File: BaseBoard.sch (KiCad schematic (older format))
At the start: 170 parts, among them Q1 MMBT2222A-7-F, Q10 IRLML6401TRPBF, Q11 MMBT2222A-7-F, Q12 IRLML6401TRPBF, Q13 MMBT2222A-7-F, Q14 IRLML6401TRPBF, Q15 MMBT2222A-7-F, Q16 IRLML6401TRPBF, Q2 IRLML6401TRPBF, Q3 MMBT2222A-7-F, Q4 IRLML6401TRPBF, Q5 MMBT2222A-7-F, Q6 IRLML6401TRPBF, Q7 MMBT2222A-7-F, Q8 IRLML6401TRPBF, Q9 MMBT2222A-7-F, U1 TLC5971PWPR, U10 TLC5971PWPR, U11 TLC5971PWPR, U12 TLC5971PWPR, U13 TLC5971PWPR, U14 TLC5971PWPR, U15 TLC5971PWPR, U16 TLC5971PWPR, U2 TLC5971PWPR, U3 TLC5971PWPR, U4 TLC5971PWPR, U5 TLC5971PWPR, U6 TLC5971PWPR, U7 TLC5971PWPR, U8 TLC5971PWPR, U9 TLC5971PWPR

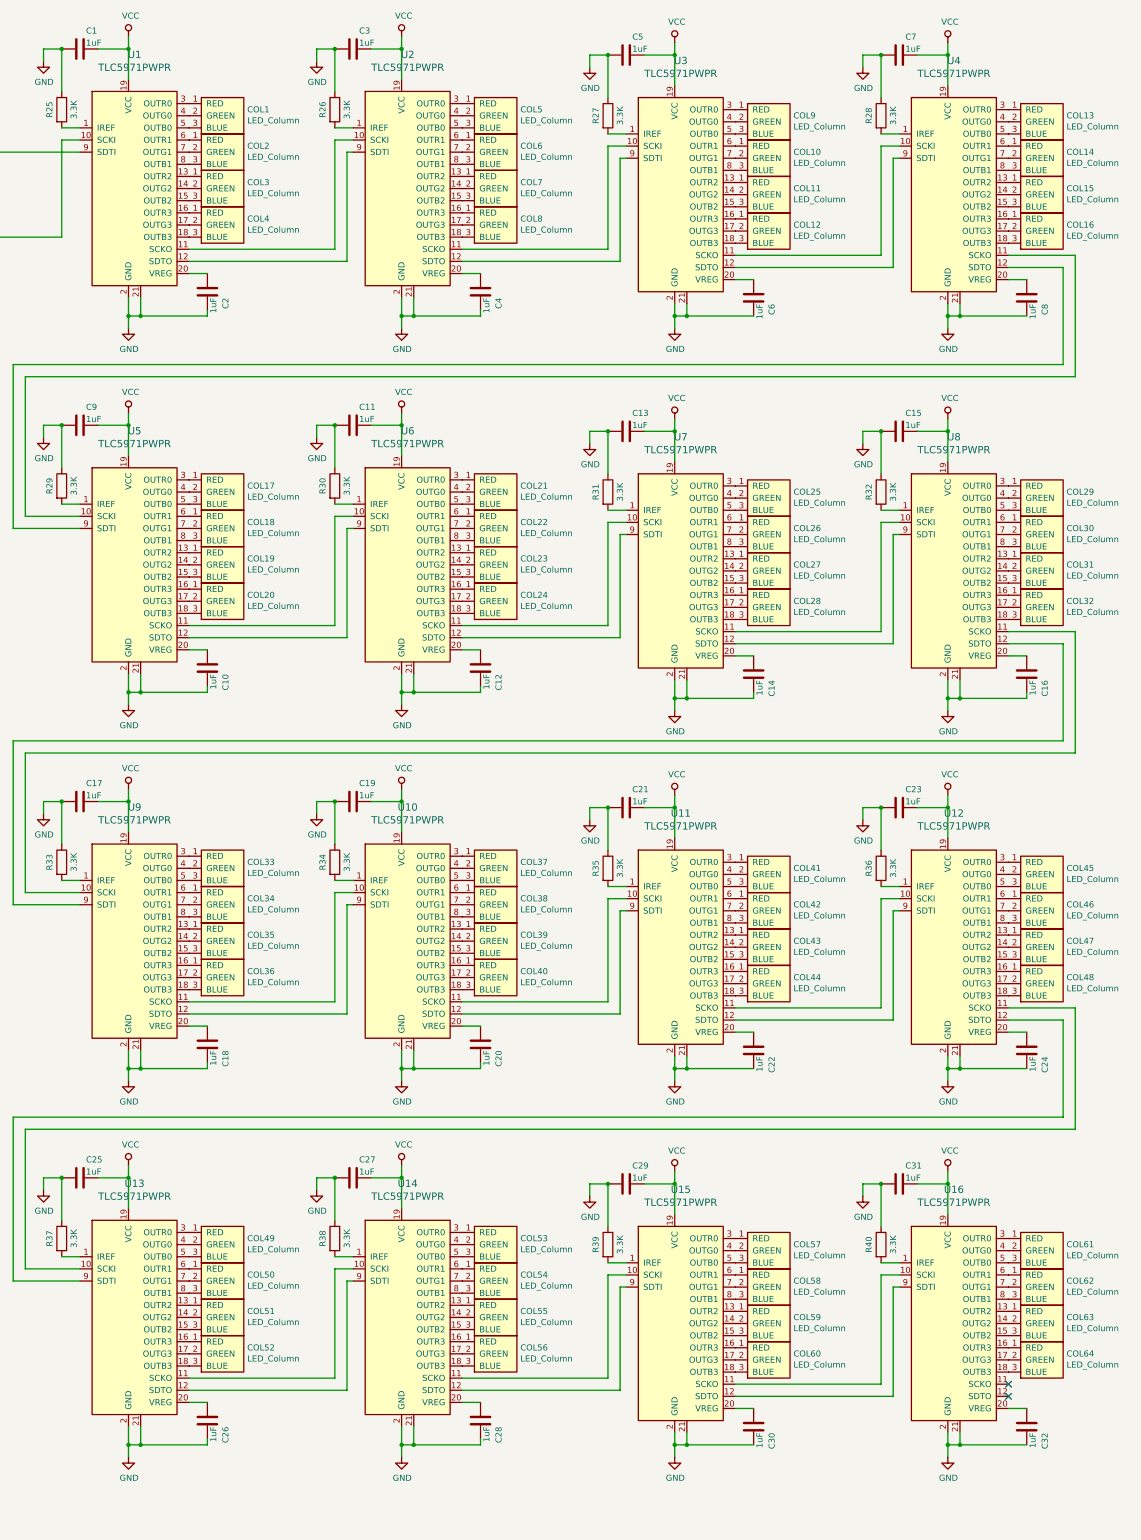
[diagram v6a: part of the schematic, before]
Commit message: Improve schematics and PCB
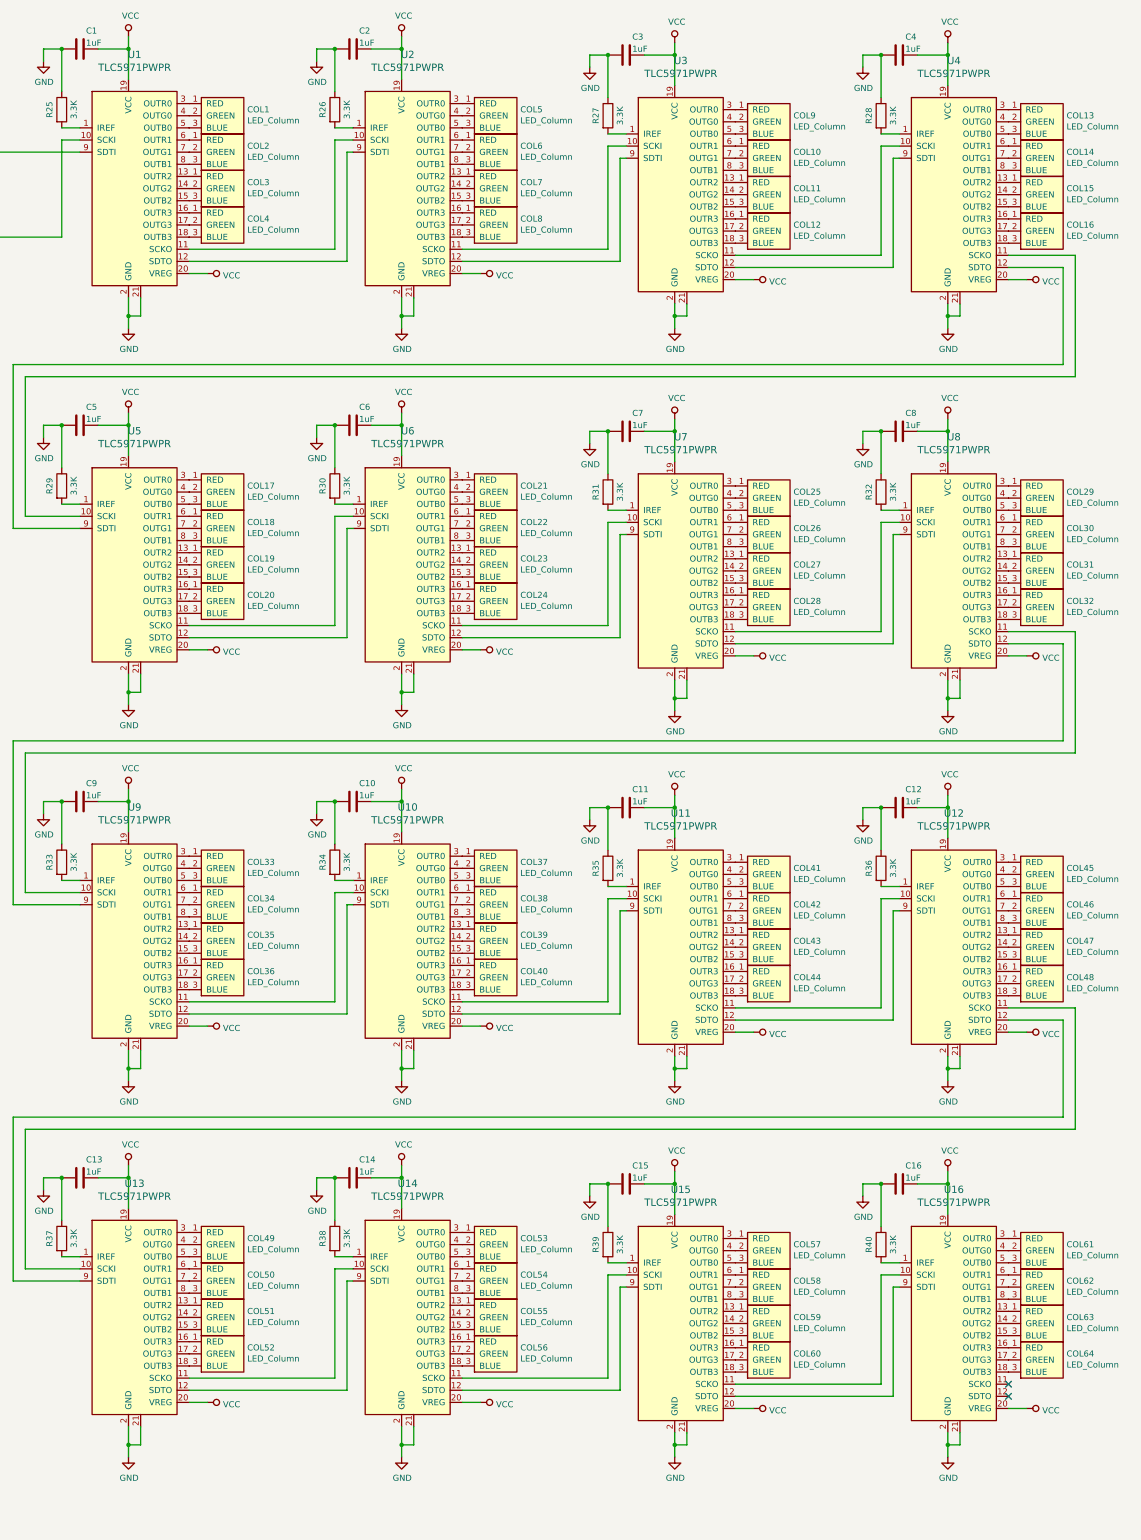
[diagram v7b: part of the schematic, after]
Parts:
- removed C10, C12, C14, C16, C18, C2, C20, C22, C24, C26, C28, C30, C32, C4, C6, C8: 1uF, Capacitor_SMD:C_0805_2012Metric_Pad1.15x1.40mm_HandSolder, symbol Device:C
- renumbered C19 to C10, C21 to C11, C23 to C12, C25 to C13, C27 to C14, C29 to C15, C31 to C16, C3 to C2, C5 to C3, C7 to C4, C9 to C5, C11 to C6, C13 to C7, C15 to C8, C17 to C9
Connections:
- net VCC: now also U1.20 (VREG), U10.20 (VREG), U11.20 (VREG), U12.20 (VREG), U13.20 (VREG), U14.20 (VREG), U15.20 (VREG), U16.20 (VREG), U2.20 (VREG), U3.20 (VREG), U4.20 (VREG), U5.20 (VREG), U6.20 (VREG), U7.20 (VREG), U8.20 (VREG), U9.20 (VREG)

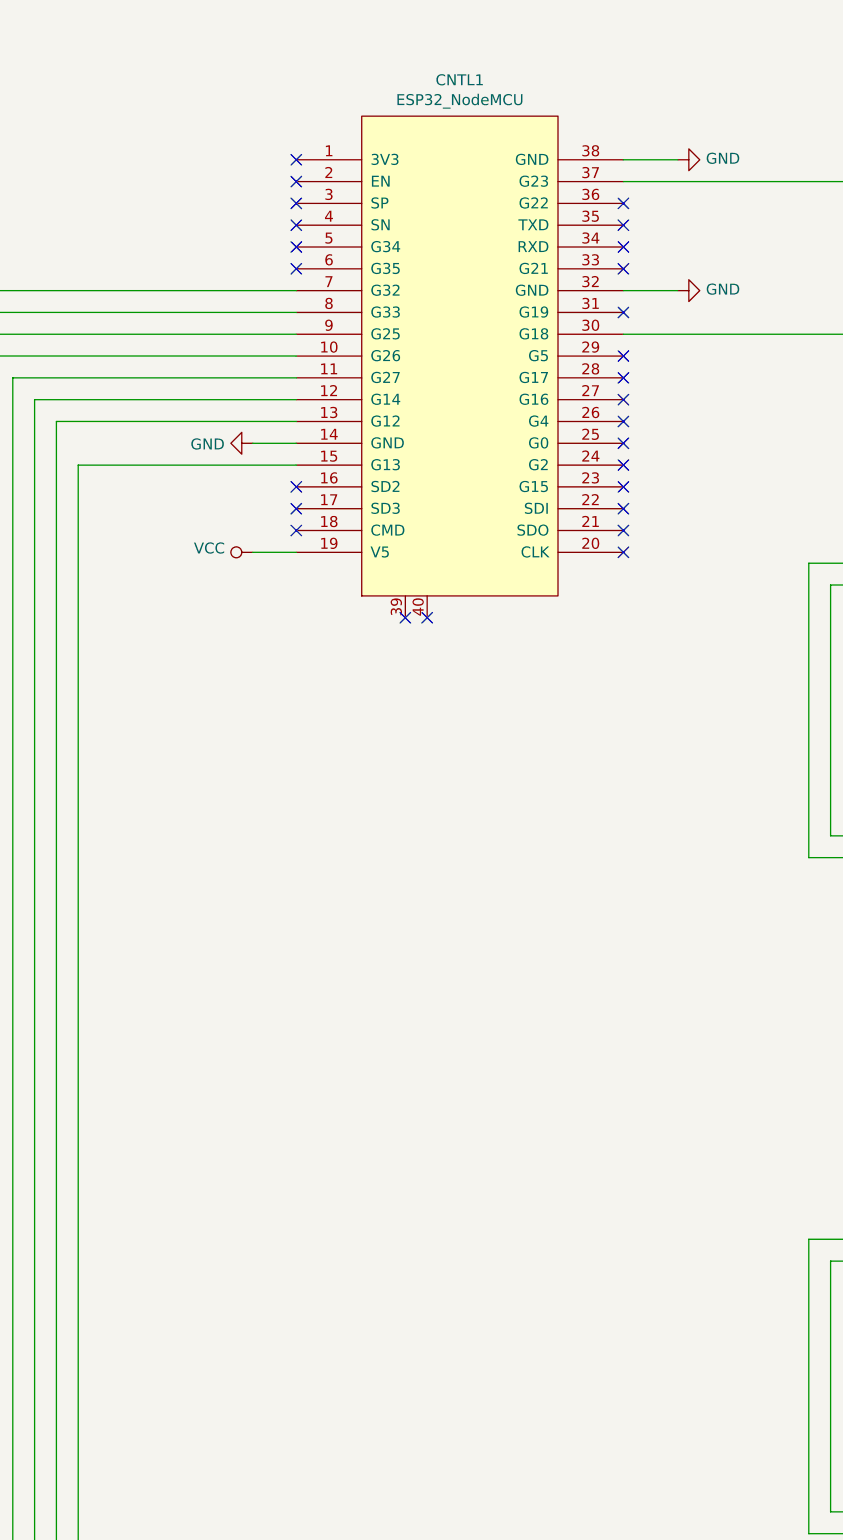
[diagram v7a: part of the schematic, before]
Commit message: Realign some components
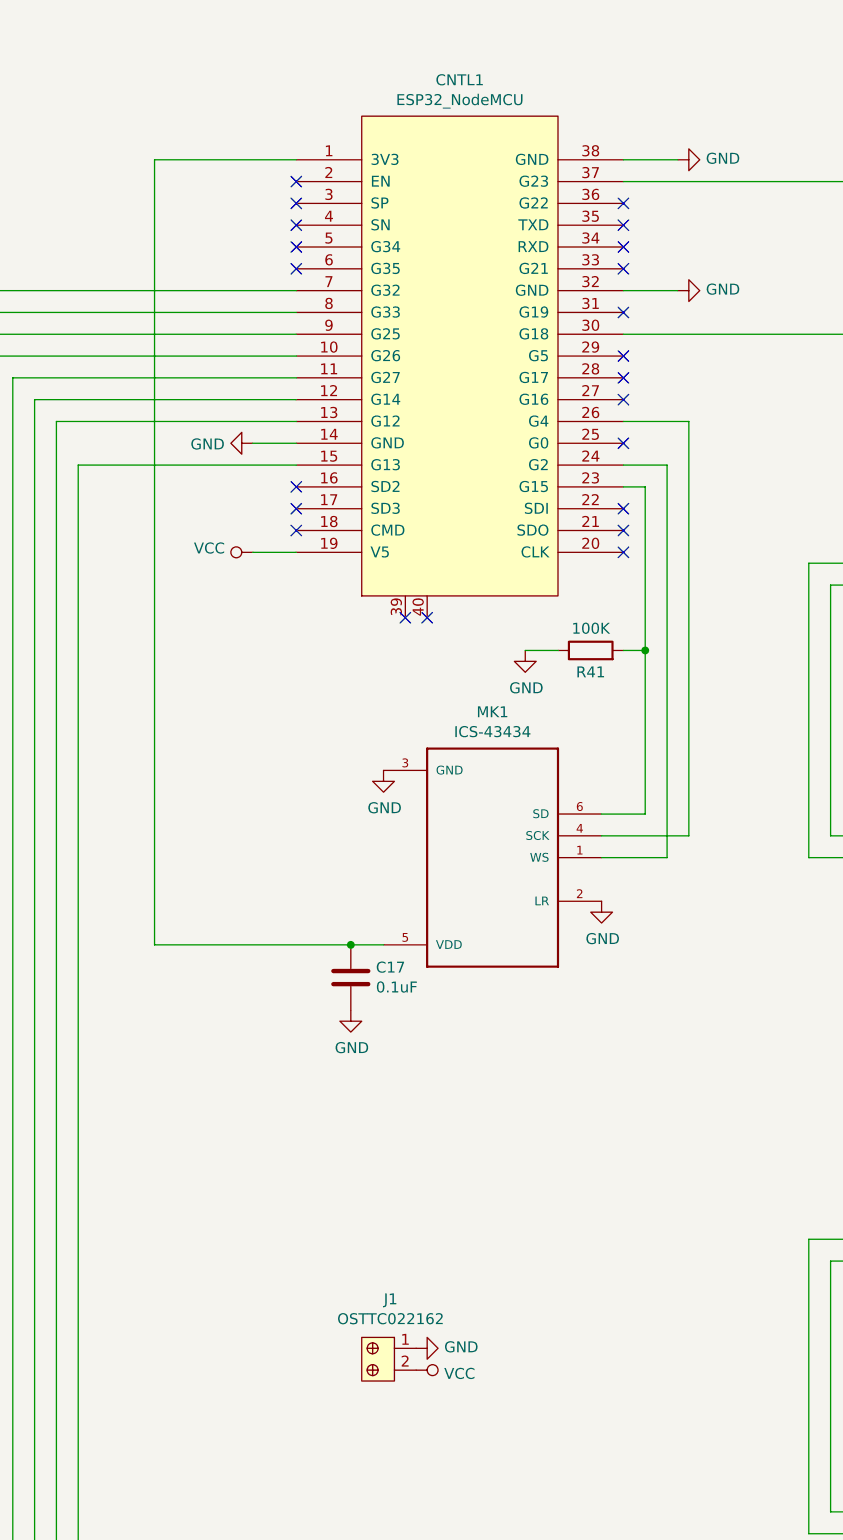
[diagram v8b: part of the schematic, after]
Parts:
- added C17: 0.1uF, Capacitor_SMD:C_0805_2012Metric_Pad1.15x1.40mm_HandSolder, symbol Device:C
- added J1: OSTTC022162, digikey-footprints:Term_Block_1x2_P5.08MM, symbol dk_Terminal-Blocks-Wire-to-Board:OSTTC022162
- added MK1: ICS-43434, BaseBoard:MIC_ICS-43434, symbol BaseBoard:ICS-43434
- added R41: 100K, Resistor_SMD:R_0805_2012Metric_Pad1.15x1.40mm_HandSolder, symbol Device:R
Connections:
- net GND: now also C17.2, J1.1, MK1.2 (LR), MK1.3 (GND), R41.1
- net VCC: now also J1.2
- net at CNTL1.1 (3V3): now also C17.1, MK1.5 (VDD)
- net at CNTL1.23 (G15): now also MK1.6 (SD), R41.2
- net at CNTL1.24 (G2): now also MK1.1 (WS)
- net at CNTL1.26 (G4): now also MK1.4 (SCK)
- no-connect marks 28 -> 24
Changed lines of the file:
@@
 $EndComp
 NoConn ~ 8050 3200
-NoConn ~ 8050 2700
 NoConn ~ 8050 2800
 NoConn ~ 8050 2900
@@
 NoConn ~ 9550 3700
 NoConn ~ 9550 3800
-NoConn ~ 9550 3900
 NoConn ~ 9550 4000
-NoConn ~ 9550 4100
-NoConn ~ 9550 4200
 NoConn ~ 9550 4300
 NoConn ~ 9550 4400
@@
 	0    1    1    0
 $EndComp
+$Comp
+L BaseBoard:ICS-43434 MK1
+U 1 1 5EBD0917
+P 8950 5900
+F 0 "MK1" H 8950 5233 50  0000 C CNN
+F 1 "ICS-43434" H 8950 5324 50  0000 C CNN
+F 2 "BaseBoard:MIC_ICS-43434" H 8950 5900 50  0001 L BNN
+F 3 "LGA-6 TDK-InvenSense" H 8950 5900 50  0001 L BNN
+F 4 "ICS-43434" H 8950 5900 50  0001 L BNN "Field4"
+F 5 "2.43 USD" H 8950 5900 50  0001 L BNN "Field5"
+F 6 "TDK-InvenSense" H 8950 5900 50  0001 L BNN "Field6"
+F 7 "Multi-Mode Microphone with I2S Digital Output" H 8950 5900 50  0001 L BNN "Field7"
+F 8 "Bad" H 8950 5900 50  0001 L BNN "Field8"
+	1    8950 5900
+	-1   0    0    1
+$EndComp
+$Comp
+L power:GND #PWR086
+U 1 1 5EBD3D7E
+P 8450 5500
+F 0 "#PWR086" H 8450 5250 50  0001 C CNN
+F 1 "GND" H 8455 5327 50  0000 C CNN
+F 2 "" H 8450 5500 50  0001 C CNN
+F 3 "" H 8450 5500 50  0001 C CNN
+	1    8450 5500
+	1    0    0    -1
+$EndComp
+Wire Wire Line
+	8050 2700 7400 2700
+Wire Wire Line
+	7400 2700 7400 6300
+Wire Wire Line
+	7400 6300 8300 6300
+$Comp
+L Device:C C17
+U 1 1 5EC0B891
+P 8300 6450
+F 0 "C17" H 8415 6496 50  0000 L CNN
+F 1 "0.1uF" H 8415 6405 50  0000 L CNN
+F 2 "Capacitor_SMD:C_0805_2012Metric_Pad1.15x1.40mm_HandSolder" H 8338 6300 50  0001 C CNN
+F 3 "~" H 8300 6450 50  0001 C CNN
+	1    8300 6450
+	1    0    0    -1
+$EndComp
+Connection ~ 8300 6300
+Wire Wire Line
+	8300 6300 8450 6300
+$Comp
+L power:GND #PWR085
+U 1 1 5EC0D5FC
+P 8300 6600
+F 0 "#PWR085" H 8300 6350 50  0001 C CNN
+F 1 "GND" H 8305 6427 50  0000 C CNN
+F 2 "" H 8300 6600 50  0001 C CNN
+F 3 "" H 8300 6600 50  0001 C CNN
+	1    8300 6600
+	1    0    0    -1
+$EndComp
+$Comp
+L power:GND #PWR087
+U 1 1 5EC0F842
+P 9450 6100
+F 0 "#PWR087" H 9450 5850 50  0001 C CNN
+F 1 "GND" H 9455 5927 50  0000 C CNN
+F 2 "" H 9450 6100 50  0001 C CNN
+F 3 "" H 9450 6100 50  0001 C CNN
+	1    9450 6100
+	1    0    0    -1
+$EndComp
+Wire Wire Line
+	9550 4200 9650 4200
+Wire Wire Line
+	9650 4200 9650 4950
+Wire Wire Line
+	9650 5700 9450 5700
+Wire Wire Line
+	9550 4100 9750 4100
+Wire Wire Line
+	9750 4100 9750 5900
+Wire Wire Line
+	9750 5900 9450 5900
+Wire Wire Line
+	9550 3900 9850 3900
+Wire Wire Line
+	9850 3900 9850 5800
+Wire Wire Line
+	9850 5800 9450 5800
+$Comp
+L Device:R R41
+U 1 1 5ECC1E09
+P 9400 4950
+F 0 "R41" V 9300 4950 50  0000 C CNN
+F 1 "100K" V 9500 4950 50  0000 C CNN
+F 2 "Resistor_SMD:R_0805_2012Metric_Pad1.15x1.40mm_HandSolder" V 9330 4950 50  0001 C CNN
+F 3 "~" H 9400 4950 50  0001 C CNN
+	1    9400 4950
+	0    -1   -1   0
+$EndComp
+Wire Wire Line
+	9550 4950 9650 4950
+Connection ~ 9650 4950
+Wire Wire Line
+	9650 4950 9650 5700
+$Comp
+L power:GND #PWR088
+U 1 1 5ED309E4
+P 9100 4950
+F 0 "#PWR088" H 9100 4700 50  0001 C CNN
+F 1 "GND" H 9105 4777 50  0000 C CNN
+F 2 "" H 9100 4950 50  0001 C CNN
+F 3 "" H 9100 4950 50  0001 C CNN
+	1    9100 4950
+	1    0    0    -1
+$EndComp
+Wire Wire Line
+	9100 4950 9250 4950
+$Comp
+L dk_Terminal-Blocks-Wire-to-Board:OSTTC022162 J1
+U 1 1 5EDDABBD
+P 8500 8150
+F 0 "J1" V 8275 8133 50  0000 C CNN
+F 1 "OSTTC022162" V 8366 8133 50  0000 C CNN
+F 2 "digikey-footprints:Term_Block_1x2_P5.08MM" H 8700 8350 60  0001 L CNN
+F 3 "http://www.on-shore.com/wp-content/uploads/OSTTCXX2162.pdf" H 8700 8450 60  0001 L CNN
+F 4 "ED2609-ND" H 8700 8550 60  0001 L CNN "Digi-Key_PN"
+F 5 "OSTTC022162" H 8700 8650 60  0001 L CNN "MPN"
+F 6 "Connectors, Interconnects" H 8700 8750 60  0001 L CNN "Category"
+F 7 "Terminal Blocks - Wire to Board" H 8700 8850 60  0001 L CNN "Family"
+F 8 "http://www.on-shore.com/wp-content/uploads/OSTTCXX2162.pdf" H 8700 8950 60  0001 L CNN "DK_Datasheet_Link"
+F 9 "/product-detail/en/on-shore-technology-inc/OSTTC022162/ED2609-ND/614558" H 8700 9050 60  0001 L CNN "DK_Detail_Page"
+F 10 "TERM BLK 2P SIDE ENT 5.08MM PCB" H 8700 9150 60  0001 L CNN "Description"
+F 11 "On Shore Technology Inc." H 8700 9250 60  0001 L CNN "Manufacturer"
+F 12 "Active" H 8700 9350 60  0001 L CNN "Status"
+	1    8500 8150
+	0    1    1    0
+$EndComp
+$Comp
+L power:GND #PWR089
+U 1 1 5EDDE8BC
+P 8600 8150
+F 0 "#PWR089" H 8600 7900 50  0001 C CNN
+F 1 "GND" V 8605 8022 50  0000 R CNN
+F 2 "" H 8600 8150 50  0001 C CNN
+F 3 "" H 8600 8150 50  0001 C CNN
+	1    8600 8150
+	0    -1   -1   0
+$EndComp
+$Comp
+L power:VCC #PWR090
+U 1 1 5EE165A0
+P 8600 8250
+F 0 "#PWR090" H 8600 8100 50  0001 C CNN
+F 1 "VCC" V 8617 8378 50  0000 L CNN
+F 2 "" H 8600 8250 50  0001 C CNN
+F 3 "" H 8600 8250 50  0001 C CNN
+	1    8600 8250
+	0    1    1    0
+$EndComp
